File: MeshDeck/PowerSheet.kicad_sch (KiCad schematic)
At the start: 21 parts, among them U3 TPS6282533DMQR, U4 BQ24074RGTR

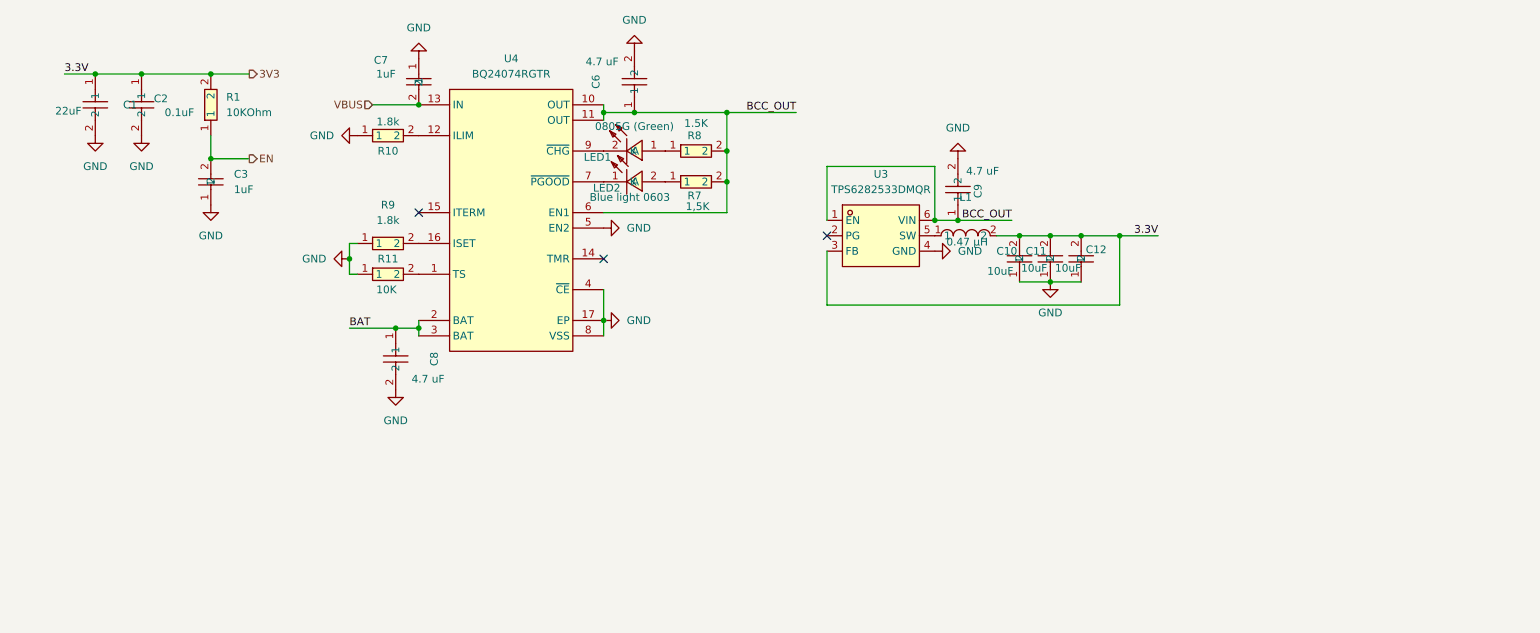
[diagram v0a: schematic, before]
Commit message: Added GPS and sof power button
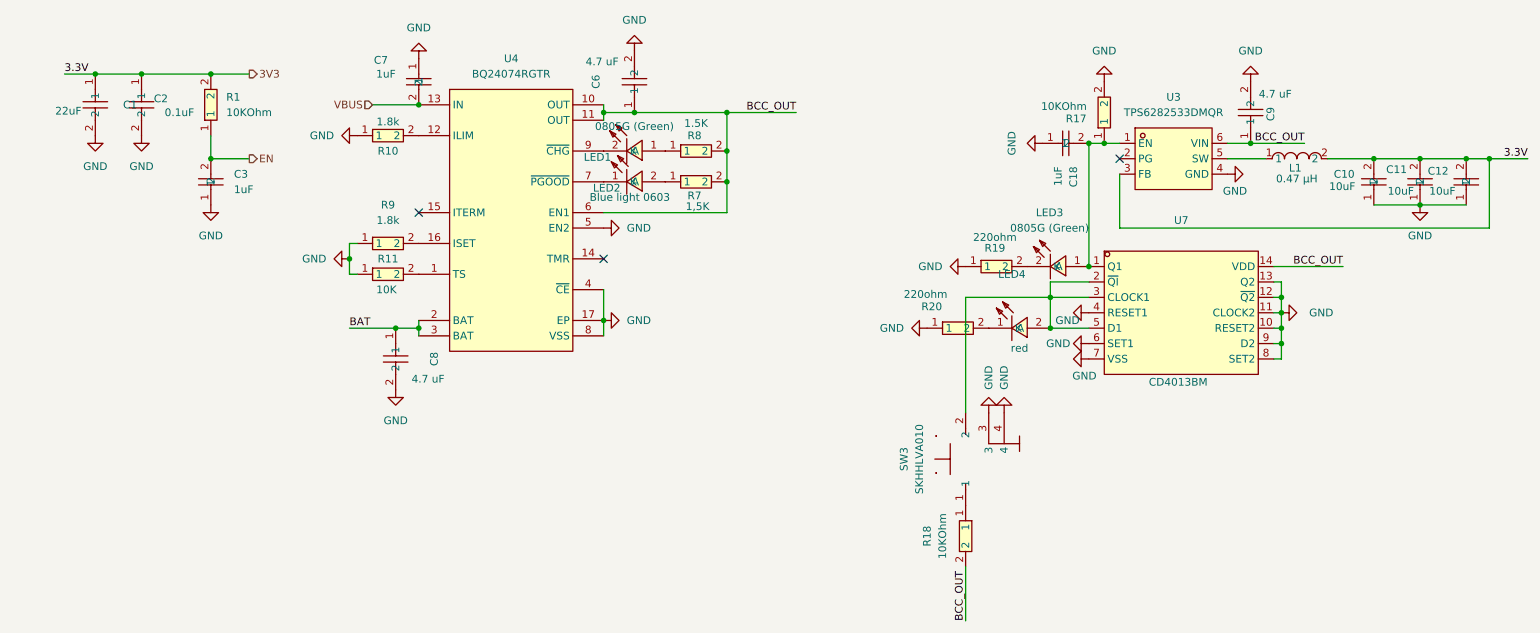
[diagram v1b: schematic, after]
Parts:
- added C18: 1uF, MeshDeck:C0402, symbol MeshDeck:CL05A105KP5NNNC
- added LED3: 0805G (Green), MeshDeck:LED0805-R-RD, symbol MeshDeck:0805G(Green)
- added LED4: red, MeshDeck:LED0402-RD, symbol MeshDeck:FC-F1005HRK-620H5
- added R17, R18: 10KOhm, MeshDeck:R0402, symbol MeshDeck:QR0402F1KQ10
- added R19, R20: 220ohm, MeshDeck:R0402, symbol MeshDeck:0402WGF2200TCE
- added SW3: SKHHLVA010, MeshDeck:KEY-TH_4P-L7.5-W6.8-P4.50-LS7.2, symbol MeshDeck:SKHHLVA010
- added U7: CD4013BM, MeshDeck:SOIC-14_L8.7-W3.9-P1.27-LS6.0-BL, symbol MeshDeck:CD4013BM
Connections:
- net BCC_OUT: now also R18.2, U7.14 (VDD); no longer U3.1 (EN)
- net GND: now also C18.1, R17.2, R19.1, R20.1, SW3.3, SW3.4, U7.10 (RESET2), U7.11 (CLOCK2), U7.12 (~{Q2}), U7.13 (Q2), U7.4 (RESET1), U7.6 (SET1), U7.7 (VSS), U7.8 (SET2), U7.9 (D2)
- new net: C18.2, LED3.1 (A), R17.1, U3.1 (EN), U7.1 (Q1)
- new net: R18.1, SW3.1
- new net: LED4.2 (A), SW3.2, U7.2 (~{QI}), U7.3 (CLOCK1), U7.5 (D1)
- new net: LED3.2 (K), R19.2
- new net: LED4.1 (K), R20.2
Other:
- moved on the sheet: C10, C11, C12, C9, L1, U3

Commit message: added sd card and started keyboard
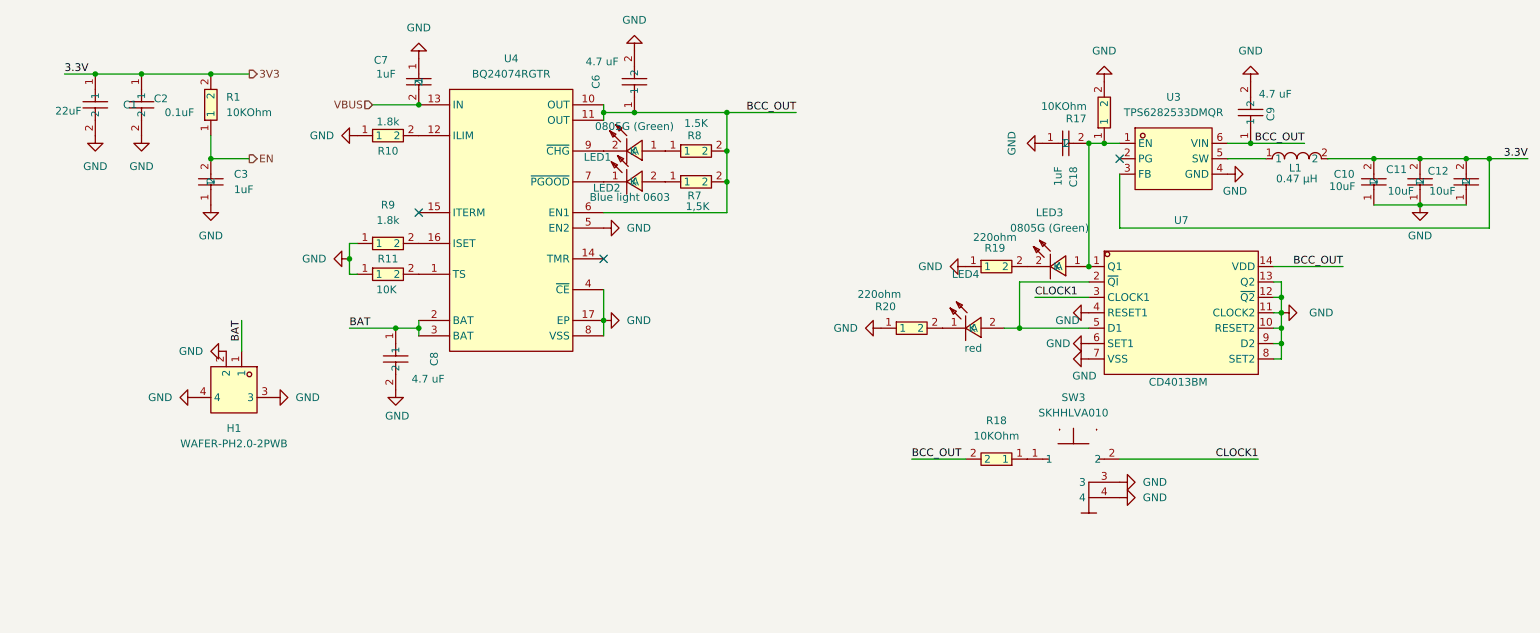
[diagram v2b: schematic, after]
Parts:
- added H1: WAFER-PH2.0-2PWB, MeshDeck:CONN-SMD_2P-P2.00_XUNPU_WAFER-PH2.0-2PWB, symbol MeshDeck:WAFER-PH2.0-2PWB
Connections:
- net BAT: now also H1.1
- net GND: now also H1.2, H1.3, H1.4
- net at LED4.2 (A), U7.2 (~{QI}), U7.5 (D1): no longer SW3.2, U7.3 (CLOCK1)
- new net CLOCK1: SW3.2, U7.3 (CLOCK1)
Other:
- moved on the sheet: LED4, R18, R20, SW3

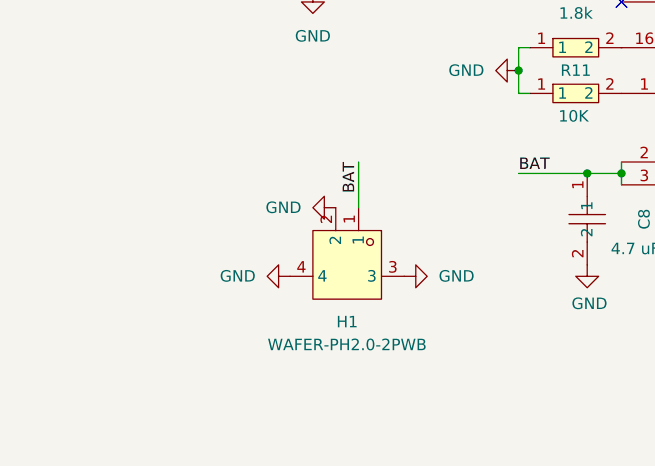
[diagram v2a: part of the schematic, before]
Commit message: started pcb plus pin socket for expansion
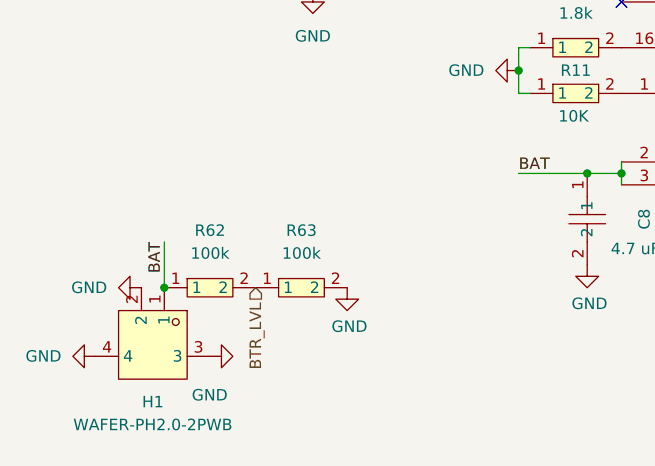
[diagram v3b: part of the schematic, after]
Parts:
- added R62, R63: 100k, MeshDeck:R0603, symbol MeshDeck:RC0603FR-07100KL
- R1, R17, R18: LCSC Part C176101 -> C25531
- R7, R8: LCSC Part C100605 -> C25867
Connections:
- net BAT: now also R62.1
- net GND: now also R63.2
- new net BTR_LVL: R62.2, R63.1
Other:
- moved on the sheet: H1
